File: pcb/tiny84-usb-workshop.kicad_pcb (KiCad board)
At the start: 2 copper layers, 61.7 x 69.9 mm, 33 parts, among them J1 Conn_02x03_Odd_Even, J2 USB_B, J3 I2C, J4 Conn_01x09, J5 Conn_01x08, SW1 BTN2, SW2 BTN1, U1 LP2950-3.3_TO92, U2 ATtiny84A-PU

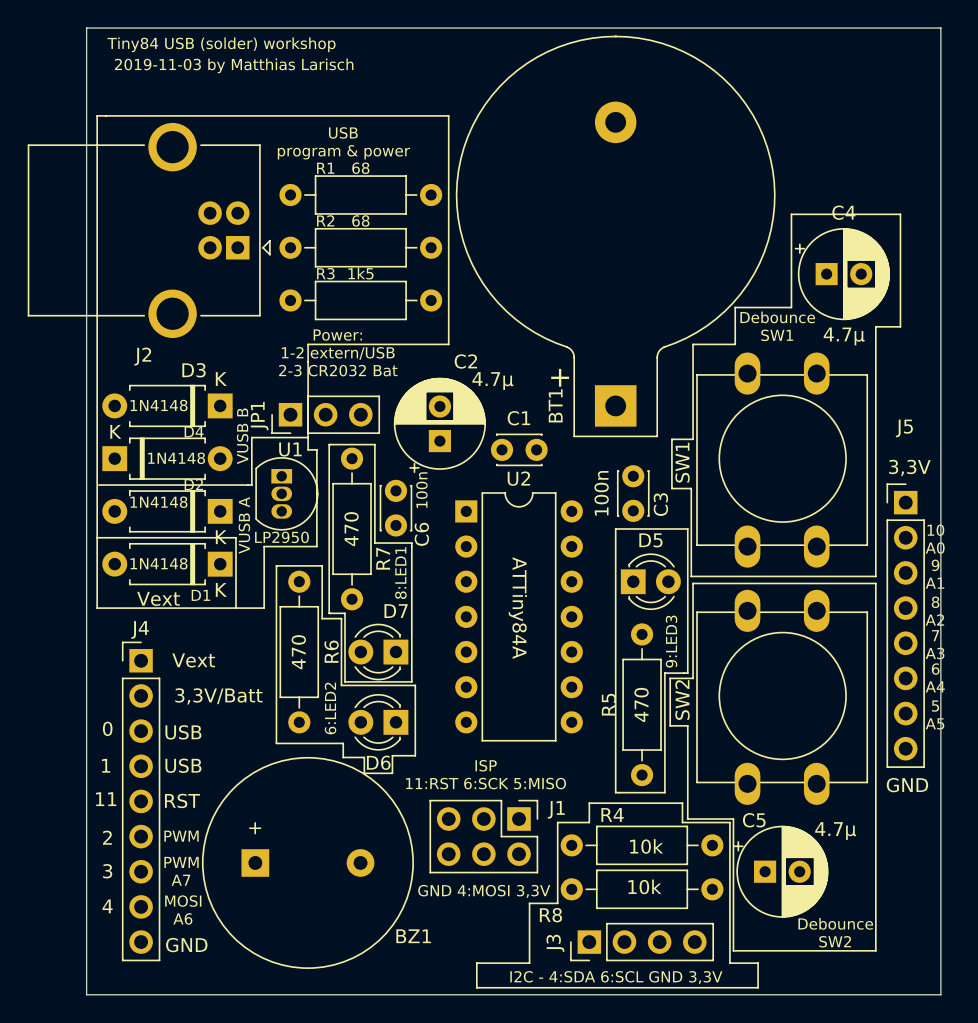
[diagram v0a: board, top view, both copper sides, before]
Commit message: silkscreen adjustments
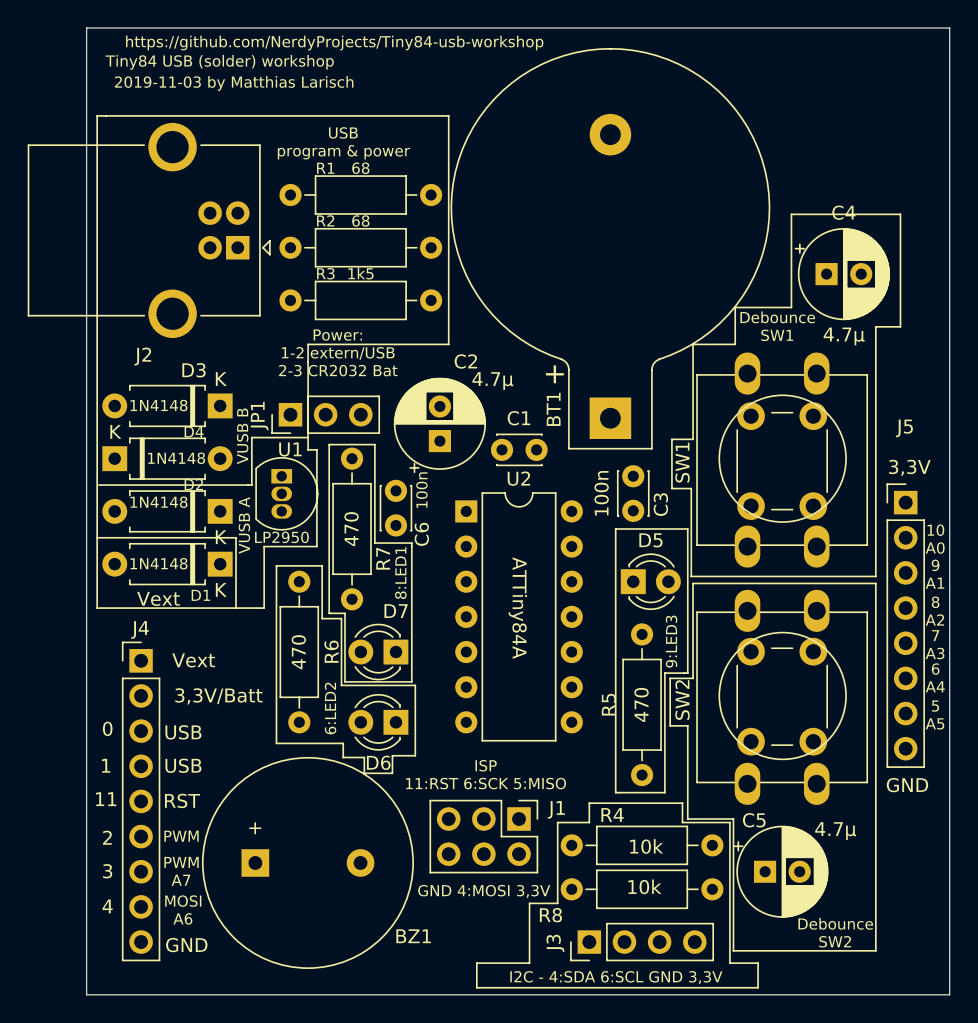
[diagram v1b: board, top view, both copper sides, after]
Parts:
- added SW3: SW_Push, Button_Switch_THT:SW_PUSH_6mm, F.Cu at (93.0, 49.8)
- added SW4: SW_Push, Button_Switch_THT:SW_PUSH_6mm, F.Cu at (93.0, 66.8)
- D5: value LED2 -> LED3
- moved BT1 0.97 mm to (82.8, 43.4)
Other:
- board size 61.7 x 69.9 mm -> 62.4 x 69.9 mm
- board text added: "https://github.com/NerdyProjects/Tiny84-usb-workshop"
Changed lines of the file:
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@@
   (general
     (thickness 1.6)
-    (drawings 133)
+    (drawings 134)
     (tracks 0)
     (zones 0)
-    (modules 33)
+    (modules 35)
     (nets 26)
   )
@@
     (add_net VDC)
   )
+  (module Button_Switch_THT:SW_PUSH_6mm (layer F.Cu)
+    (at 92.964 66.802 90)
+    (descr https://www.omron.com/ecb/products/pdf/en-b3f.pdf)
+    (tags "tact sw push 6mm")
+    (fp_text reference SW4 (at 3.25 -2 90) (layer F.SilkS) hide
+      (effects (font (size 1 1) (thickness 0.15)))
+    )
+    (fp_text value SW_Push (at 3.75 6.7 90) (layer F.Fab)
+      (effects (font (size 1 1) (thickness 0.15)))
+    )
+    (fp_circle (center 3.25 2.25) (end 1.25 2.5) (layer F.Fab) (width 0.1))
+    (fp_line (start 6.75 3) (end 6.75 1.5) (layer F.SilkS) (width 0.12))
+    (fp_line (start 5.5 -1) (end 1 -1) (layer F.SilkS) (width 0.12))
+    (fp_line (start -0.25 1.5) (end -0.25 3) (layer F.SilkS) (width 0.12))
+    (fp_line (start 1 5.5) (end 5.5 5.5) (layer F.SilkS) (width 0.12))
+    (fp_line (start 8 -1.25) (end 8 5.75) (layer F.CrtYd) (width 0.05))
+    (fp_line (start 7.75 6) (end -1.25 6) (layer F.CrtYd) (width 0.05))
+    (fp_line (start -1.5 5.75) (end -1.5 -1.25) (layer F.CrtYd) (width 0.05))
+    (fp_line (start -1.25 -1.5) (end 7.75 -1.5) (layer F.CrtYd) (width 0.05))
+    (fp_line (start -1.5 6) (end -1.25 6) (layer F.CrtYd) (width 0.05))
+    (fp_line (start -1.5 5.75) (end -1.5 6) (layer F.CrtYd) (width 0.05))
+    (fp_line (start -1.5 -1.5) (end -1.25 -1.5) (layer F.CrtYd) (width 0.05))
+    (fp_line (start -1.5 -1.25) (end -1.5 -1.5) (layer F.CrtYd) (width 0.05))
+    (fp_line (start 8 -1.5) (end 8 -1.25) (layer F.CrtYd) (width 0.05))
+    (fp_line (start 7.75 -1.5) (end 8 -1.5) (layer F.CrtYd) (width 0.05))
+    (fp_line (start 8 6) (end 8 5.75) (layer F.CrtYd) (width 0.05))
+    (fp_line (start 7.75 6) (end 8 6) (layer F.CrtYd) (width 0.05))
+    (fp_line (start 0.25 -0.75) (end 3.25 -0.75) (layer F.Fab) (width 0.1))
+    (fp_line (start 0.25 5.25) (end 0.25 -0.75) (layer F.Fab) (width 0.1))
+    (fp_line (start 6.25 5.25) (end 0.25 5.25) (layer F.Fab) (width 0.1))
+    (fp_line (start 6.25 -0.75) (end 6.25 5.25) (layer F.Fab) (width 0.1))
+    (fp_line (start 3.25 -0.75) (end 6.25 -0.75) (layer F.Fab) (width 0.1))
+    (fp_text user %R (at 3.25 2.25 90) (layer F.Fab)
+      (effects (font (size 1 1) (thickness 0.15)))
+    )
+    (pad 1 thru_hole circle (at 6.5 0 180) (size 2 2) (drill 1.1) (layers *.Cu *.Mask)
+      (net 23 PA2))
+    (pad 2 thru_hole circle (at 6.5 4.5 180) (size 2 2) (drill 1.1) (layers *.Cu *.Mask)
+      (net 2 GND))
+    (pad 1 thru_hole circle (at 0 0 180) (size 2 2) (drill 1.1) (layers *.Cu *.Mask)
+      (net 23 PA2))
+    (pad 2 thru_hole circle (at 0 4.5 180) (size 2 2) (drill 1.1) (layers *.Cu *.Mask)
+      (net 2 GND))
+    (model ${KISYS3DMOD}/Button_Switch_THT.3dshapes/SW_PUSH_6mm.wrl
+      (at (xyz 0 0 0))
+      (scale (xyz 1 1 1))
+      (rotate (xyz 0 0 0))
+    )
+  )
+  (module Button_Switch_THT:SW_PUSH_6mm (layer F.Cu)
+    (at 92.964 49.784 90)
+    (descr https://www.omron.com/ecb/products/pdf/en-b3f.pdf)
+    (tags "tact sw push 6mm")
+    (fp_text reference SW3 (at 3.25 -2 90) (layer F.SilkS) hide
+      (effects (font (size 1 1) (thickness 0.15)))
+    )
+    (fp_text value SW_Push (at 3.75 6.7 90) (layer F.Fab)
+      (effects (font (size 1 1) (thickness 0.15)))
+    )
+    (fp_circle (center 3.25 2.25) (end 1.25 2.5) (layer F.Fab) (width 0.1))
+    (fp_line (start 6.75 3) (end 6.75 1.5) (layer F.SilkS) (width 0.12))
+    (fp_line (start 5.5 -1) (end 1 -1) (layer F.SilkS) (width 0.12))
+    (fp_line (start -0.25 1.5) (end -0.25 3) (layer F.SilkS) (width 0.12))
+    (fp_line (start 1 5.5) (end 5.5 5.5) (layer F.SilkS) (width 0.12))
+    (fp_line (start 8 -1.25) (end 8 5.75) (layer F.CrtYd) (width 0.05))
+    (fp_line (start 7.75 6) (end -1.25 6) (layer F.CrtYd) (width 0.05))
+    (fp_line (start -1.5 5.75) (end -1.5 -1.25) (layer F.CrtYd) (width 0.05))
+    (fp_line (start -1.25 -1.5) (end 7.75 -1.5) (layer F.CrtYd) (width 0.05))
+    (fp_line (start -1.5 6) (end -1.25 6) (layer F.CrtYd) (width 0.05))
+    (fp_line (start -1.5 5.75) (end -1.5 6) (layer F.CrtYd) (width 0.05))
+    (fp_line (start -1.5 -1.5) (end -1.25 -1.5) (layer F.CrtYd) (width 0.05))
+    (fp_line (start -1.5 -1.25) (end -1.5 -1.5) (layer F.CrtYd) (width 0.05))
+    (fp_line (start 8 -1.5) (end 8 -1.25) (layer F.CrtYd) (width 0.05))
+    (fp_line (start 7.75 -1.5) (end 8 -1.5) (layer F.CrtYd) (width 0.05))
+    (fp_line (start 8 6) (end 8 5.75) (layer F.CrtYd) (width 0.05))
+    (fp_line (start 7.75 6) (end 8 6) (layer F.CrtYd) (width 0.05))
+    (fp_line (start 0.25 -0.75) (end 3.25 -0.75) (layer F.Fab) (width 0.1))
+    (fp_line (start 0.25 5.25) (end 0.25 -0.75) (layer F.Fab) (width 0.1))
+    (fp_line (start 6.25 5.25) (end 0.25 5.25) (layer F.Fab) (width 0.1))
+    (fp_line (start 6.25 -0.75) (end 6.25 5.25) (layer F.Fab) (width 0.1))
+    (fp_line (start 3.25 -0.75) (end 6.25 -0.75) (layer F.Fab) (width 0.1))
+    (fp_text user %R (at 3.25 2.25 90) (layer F.Fab)
+      (effects (font (size 1 1) (thickness 0.15)))
+    )
+    (pad 1 thru_hole circle (at 6.5 0 180) (size 2 2) (drill 1.1) (layers *.Cu *.Mask)
+      (net 22 PA3))
+    (pad 2 thru_hole circle (at 6.5 4.5 180) (size 2 2) (drill 1.1) (layers *.Cu *.Mask)
+      (net 2 GND))
+    (pad 1 thru_hole circle (at 0 0 180) (size 2 2) (drill 1.1) (layers *.Cu *.Mask)
+      (net 22 PA3))
+    (pad 2 thru_hole circle (at 0 4.5 180) (size 2 2) (drill 1.1) (layers *.Cu *.Mask)
+      (net 2 GND))
+    (model ${KISYS3DMOD}/Button_Switch_THT.3dshapes/SW_PUSH_6mm.wrl
+      (at (xyz 0 0 0))
+      (scale (xyz 1 1 1))
+      (rotate (xyz 0 0 0))
+    )
+  )
   (module Capacitor_THT:C_Disc_D3.0mm_W2.0mm_P2.50mm (layer F.Cu)
     (at 67.31 51.181 90)
@@
       (effects (font (size 1 1) (thickness 0.15)))
     )
-    (fp_text value LED2 (at 1.27 2.96) (layer F.Fab)
+    (fp_text value LED3 (at 1.27 2.96) (layer F.Fab)
       (effects (font (size 1 1) (thickness 0.15)))
     )
@@
   )
   (module Battery:BatteryHolder_Keystone_103_1x20mm (layer F.Cu)
-    (at 83.185 42.545 90)
+    (at 82.804 43.434 90)
     (descr http://www.keyelco.com/product-pdf.cfm?p=719)
     (tags "Keystone type 103 battery holder")
-    (fp_text reference BT1 (at 0 -4.3 90) (layer F.SilkS)
+    (fp_text reference BT1 (at 0.635 -4.064 90) (layer F.SilkS)
       (effects (font (size 1 1) (thickness 0.15)))
     )
@@
       (effects (font (size 1 1) (thickness 0.15)))
     )
-    (fp_text user + (at 2.032 -4.064 90) (layer F.SilkS)
+    (fp_text user + (at 3.175 -4.064 90) (layer F.SilkS)
       (effects (font (size 1.5 1.5) (thickness 0.15)))
     )
@@
     )
   )
-  (gr_text "2019-11-03 by Matthias Larisch" (at 55.626 17.907) (layer F.SilkS)
+  (gr_text https://github.com/NerdyProjects/Tiny84-usb-workshop (at 62.865 16.256) (layer F.SilkS)
     (effects (font (size 0.8 0.8) (thickness 0.15)))
   )
-  (gr_text "Tiny84 USB (solder) workshop" (at 54.737 16.383) (layer F.SilkS)
+  (gr_text "2019-11-03 by Matthias Larisch" (at 55.626 19.177) (layer F.SilkS)
     (effects (font (size 0.8 0.8) (thickness 0.15)))
   )
+  (gr_text "Tiny84 USB (solder) workshop" (at 54.61 17.653) (layer F.SilkS)
+    (effects (font (size 0.8 0.8) (thickness 0.15)))
+  )
   (gr_line (start 44.958 15.24) (end 44.958 85.09) (layer Edge.Cuts) (width 0.05))
-  (gr_line (start 106.68 15.24) (end 44.958 15.24) (layer Edge.Cuts) (width 0.05))
-  (gr_line (start 106.68 85.09) (end 106.68 15.24) (layer Edge.Cuts) (width 0.05))
-  (gr_line (start 44.958 85.09) (end 106.68 85.09) (layer Edge.Cuts) (width 0.05))
+  (gr_line (start 107.315 15.24) (end 44.958 15.24) (layer Edge.Cuts) (width 0.05))
+  (gr_line (start 107.315 85.09) (end 107.315 15.24) (layer Edge.Cuts) (width 0.05))
+  (gr_line (start 44.958 85.09) (end 107.315 85.09) (layer Edge.Cuts) (width 0.05))
   (gr_text 0 (at 46.482 65.913) (layer F.SilkS)
     (effects (font (size 1 1) (thickness 0.15)))

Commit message: finish pcb v1
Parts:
- added D8: ZF 3,3, Diode_THT:D_DO-35_SOD27_P7.62mm_Horizontal, F.Cu at (59.7, 24.4)
- added D9: ZF 3,3, Diode_THT:D_DO-35_SOD27_P7.62mm_Horizontal, F.Cu at (59.7, 21.8)
- added REF**: TO-92L_HandSolder, Package_TO_SOT_THT:TO-92L_HandSolder, F.Cu at (101.6, 53.3)
- added REF**: TO-92L_HandSolder, Package_TO_SOT_THT:TO-92L_HandSolder, F.Cu at (101.6, 63.5)
- added REF**: OSHW-Logo2_7.3x6mm_SilkScreen, Symbol:OSHW-Logo2_7.3x6mm_SilkScreen, F.Cu at (69.5, 82.0)
- moved SW3 20.6 mm to (98.6, 30.0)
- moved SW1 20.5 mm to (98.4, 33.0)
- moved SW4 13.4 mm to (98.7, 78.9)
- moved J5 13.3 mm to (91.4, 45.7)
- moved SW2 13.2 mm to (98.4, 81.8)
- moved C4 8.59 mm to (93.6, 40.1), turned to 180 degrees
- moved C5 6.87 mm to (91.1, 70.0), turned to 90 degrees
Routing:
- net +3V3: track 0.00 -> 160.6 mm, vias 0 -> 2
- net USB_D+: track 0.00 -> 59.9 mm
- net PA2: track 0.00 -> 56.1 mm
- net RESET: track 0.00 -> 54.8 mm
- net PA3: track 0.00 -> 54.8 mm
- net USB_D-: track 0.00 -> 52.7 mm
- net MOSI: track 0.00 -> 50.8 mm
- net PA7: track 0.00 -> 45.9 mm
- net SCK: track 0.00 -> 42.2 mm
- net PB2: track 0.00 -> 30.2 mm
- net Net-(D2-Pad2): track 0.00 -> 26.7 mm
- net MISO: track 0.00 -> 21.8 mm
- net Net-(BT1-Pad1): track 0.00 -> 21.4 mm, vias 0 -> 2
- net GND: track 0.00 -> 16.6 mm, vias 0 -> 4
- net Net-(D9-Pad1): track 0.00 -> 14.6 mm
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- added copper zone on B.Cu, net GND
- added copper zone on F.Cu, net GND
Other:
- board text added: "Experiment area"
- board text added: "Minimum component list: C1 100 nF ceramic capacitor C2 4.7µF polarised electrolytic capacitor D7 3mm LED (red, green, yellow, your choice) R7 470 ohms (100-1000) JP1 3 pin header + jumper put on 2-3 U2 14 pin socket + ATTiny84A microcontroller BT1 battery holder + 3V CR2032 (last)"
- board text added: "Power: 1-2 extern/USB 2-3 CR2032 Bat 1 2 3"
- board text added: "Take care when connecting external hardware. Board operat es with 3.3V normally. Applying 5V might break something. Especially the computers USB port."
- board text added: "Thank you for opening yourself to the world of electronics. Please start by putting all the components from the minimum component list onto the other side of this board and solder them on. Ask for support and don't feel bad for any mistakes you might do - we all did and still"
- board text added: "With the default program, the battery will last for about 10 days of continuous operation. Please turn the device off when you don't need it. This board can be programmed using the Arduino IDE. See the homepage on front for details. Still, this board is not meant for daily development work. Consider buying an Arduino Uno or Nano for that."
- board text added: "do them. Insert the battery as a last step after checking all components are properly placed. The LED1 should show your success :-)"
- board text removed: "Power: 1-2 extern/USB 2-3 CR2032 Bat"

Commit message: fix voltage regulator caps
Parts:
- removed REF** (x2): TO-92L_HandSolder, Package_TO_SOT_THT:TO-92L_HandSolder
- removed REF**: OSHW-Logo2_7.3x6mm_SilkScreen, Symbol:OSHW-Logo2_7.3x6mm_SilkScreen
- added C7: 4.7µ, Capacitor_THT:CP_Radial_D6.3mm_P2.50mm, F.Cu at (55.4, 57.8)
- added C8: 100n, Capacitor_THT:C_Disc_D3.0mm_W2.0mm_P2.50mm, F.Cu at (59.6, 37.6)
- SW1: value BTN2 -> BTN1
- SW2: value BTN1 -> BTN2
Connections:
- C4 pad 1: PA3 -> PB2
- D7 pad 1: PB2 -> PA3
- SW1 pad 1: PA3 -> PB2
- SW3 pad 1: PA3 -> PB2
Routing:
- net PB2: track 30.2 -> 84.3 mm
- net Net-(C8-Pad1): track 10.1 -> 58.6 mm
- net PA3: track 54.8 -> 31.3 mm
- net Net-(C7-Pad1): track 8.26 -> 12.4 mm
- net +3V3: track 160.6 -> 163.7 mm
- net GND: vias 4 -> 12
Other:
- board text added: "2 PB2"
- board text added: "4:LED2"
- board text added: "7:LED1"
- board text added: "8 PA2"
- board text added: "LED"
- board text added: "PWM SW1"
- board text added: "Power: 1-2 extern/USB 2-3 Battery 1 2 3"
- board text removed: "6:LED2"
- board text removed: "8:LED1"
- board text removed: "PWM"
- board text removed: "Power: 1-2 extern/USB 2-3 CR2032 Bat 1 2 3"

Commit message: PCB + errata
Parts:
- added Q1: BC547, Package_TO_SOT_THT:TO-92_Inline, F.Cu at (104.1, 53.4)
- added Q2: BC547, Package_TO_SOT_THT:TO-92_Inline, F.Cu at (104.1, 63.6)
